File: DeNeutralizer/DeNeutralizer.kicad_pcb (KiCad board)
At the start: 2 copper layers, 27.9 x 72 mm, 21 parts, among them J1 Screw_Terminal_01x03, J2 Screw_Terminal_01x03, J3 Screw_Terminal_01x03, J4 Screw_Terminal_01x03, J5 Screw_Terminal_01x02, J6 Screw_Terminal_01x05, J7 Screw_Terminal_01x02, J8 Conn_01x02_Male, J9 Ripple-Cap, U1 PC817

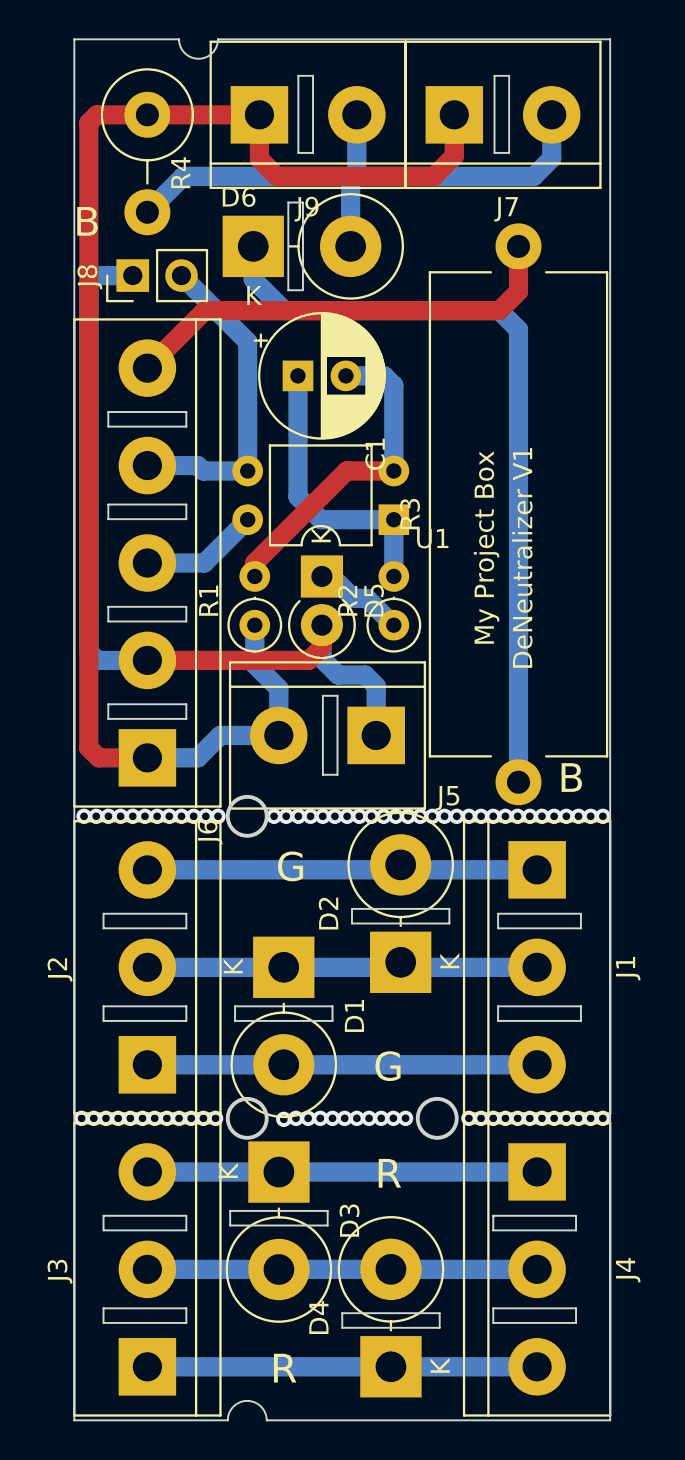
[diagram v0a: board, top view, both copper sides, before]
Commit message: Add Shelly 1 to the 3D model export
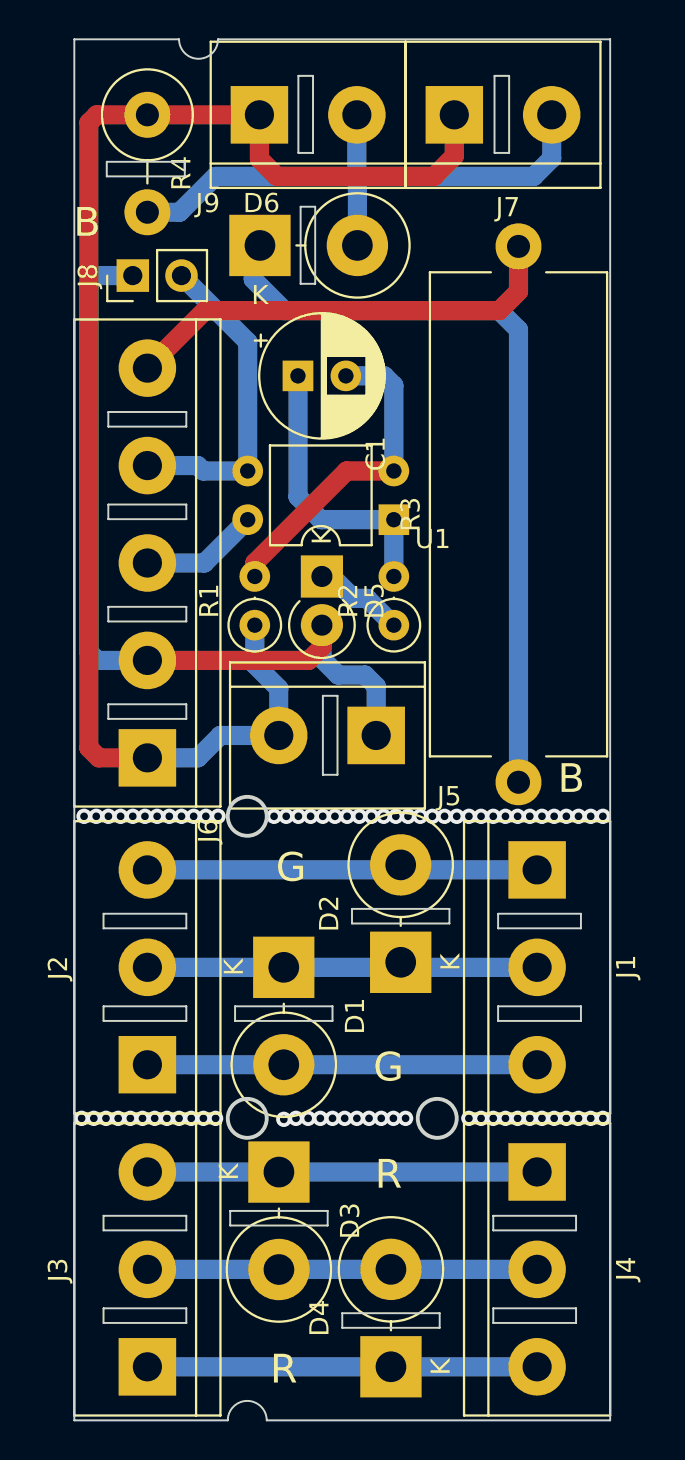
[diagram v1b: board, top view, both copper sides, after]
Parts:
- moved D6 0.35 mm to (126.5, 79.2)
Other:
- outline, holes or cut-outs redrawn
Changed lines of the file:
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@@
   (net 16 "Net-(J6-Pad4)")
   (footprint "Diode_THT:D_DO-201AD_P5.08mm_Vertical_KathodeUp" (layer "F.Cu")
-    (at 126.17 79.25)
+    (at 126.52 79.2)
     (descr "Diode, DO-201AD series, Axial, Vertical, pin pitch=5.08mm, , length*diameter=9.5*5.2mm^2, , http://www.diodes.com/_files/packages/DO-201AD.pdf")
     (tags "Diode DO-201AD series Axial Vertical pin pitch 5.08mm  length 9.5mm diameter 5.2mm")
@@
     (property "Sheetname" "")
     (attr through_hole)
-    (fp_text reference "D6" (at -0.762 -2.54) (layer "F.SilkS")
+    (fp_text reference "D6" (at 0.08 -2.2) (layer "F.SilkS")
       (effects (font (size 1 1) (thickness 0.15)))
     )
@@
       (effects (font (size 1 1) (thickness 0.15)))
     )
-    (fp_text user "${REFERENCE}" (at -0.762 -2.54) (layer "F.Fab")
+    (fp_text user "${REFERENCE}" (at 0.08 -2.2) (layer "F.Fab")
       (effects (font (size 1 1) (thickness 0.15)))
     )
@@
       (rotate (xyz 0 0 0))
     )
+    (model "C:/Users/POLYGONTeam/Desktop/Shelly_1_PM_Rund.stp"
+      (offset (xyz 10 25 15))
+      (scale (xyz 1 1 1))
+      (rotate (xyz 90 0 0))
+    )
   )
   (footprint "Diode_THT:D_DO-201AD_P5.08mm_Vertical_KathodeUp" (layer "F.Cu")
@@
     (property "Sheetname" "")
     (attr through_hole)
-    (fp_text reference "J9" (at 2.54 4.826) (layer "F.SilkS")
+    (fp_text reference "J9" (at -2.692 4.61) (layer "F.SilkS")
       (effects (font (size 1 1) (thickness 0.15)))
     )
@@
       (effects (font (size 1 1) (thickness 0.15)))
     )
-    (fp_text user "${REFERENCE}" (at 2.54 4.826) (layer "F.Fab")
+    (fp_text user "${REFERENCE}" (at -2.692 4.61) (layer "F.Fab")
       (effects (font (size 1 1) (thickness 0.15)))
     )
@@
   (gr_rect (start 138.684 134.62) (end 143.002 135.382) (layer "Edge.Cuts") (width 0.1) (fill none))
   (gr_rect (start 138.75 74.376) (end 139.512 70.358) (layer "Edge.Cuts") (width 0.1) (fill none))
+  (gr_rect (start 128.638 81.2) (end 129.4 77.182) (layer "Edge.Cuts") (width 0.1) (fill none))
   (gr_rect (start 118.364 134.62) (end 122.682 135.382) (layer "Edge.Cuts") (width 0.1) (fill none))
   (gr_line (start 124.841 140.462) (end 116.84 140.462) (layer "Edge.Cuts") (width 0.1))
@@
   (gr_circle (center 125.857 108.966) (end 126.873 108.966) (layer "Edge.Cuts") (width 0.2) (fill none))
   (gr_rect (start 130.81 134.874) (end 135.89 135.636) (layer "Edge.Cuts") (width 0.1) (fill none))
-  (gr_rect (start 128 81.536) (end 128.762 76.964) (layer "Edge.Cuts") (width 0.1) (fill none))
   (gr_rect (start 138.938 114.046) (end 143.256 114.808) (layer "Edge.Cuts") (width 0.1) (fill none))
   (gr_rect (start 118.364 114.046) (end 122.682 114.808) (layer "Edge.Cuts") (width 0.1) (fill none))
@@
   (gr_rect (start 125.222 118.872) (end 130.302 119.634) (layer "Edge.Cuts") (width 0.1) (fill none))
   (gr_rect (start 118.614 103.124) (end 122.682 103.886) (layer "Edge.Cuts") (width 0.1) (fill none))
+  (gr_rect (start 118.532 74.838) (end 122.6 75.6) (layer "Edge.Cuts") (width 0.1) (fill none))
   (gr_line (start 144.78 68.453) (end 124.333 68.453) (layer "Edge.Cuts") (width 0.1))
   (gr_rect (start 129.8 106.8) (end 130.562 102.682) (layer "Edge.Cuts") (width 0.1) (fill none))
@@
   (gr_rect (start 118.614 98.044) (end 122.682 98.806) (layer "Edge.Cuts") (width 0.1) (fill none))
   (gr_circle (center 135.763 124.714) (end 136.779 124.714) (layer "Edge.Cuts") (width 0.2) (fill none))
+  (gr_text "DeNeutralizer V1" (at 140.25 95.5 90) (layer "B.SilkS")
+    (effects (font (size 1 1) (thickness 0.25)) (justify mirror))
+  )
   (gr_text "N" (at 128.8 107.6) (layer "B.SilkS")
     (effects (font (size 1.5 1.5) (thickness 0.3)) (justify mirror))
@@
     (effects (font (size 1.5 1.5) (thickness 0.3)) (justify mirror))
   )
+  (gr_text "My Project Box" (at 138.25 95 90) (layer "B.SilkS")
+    (effects (font (size 1 1) (thickness 0.25)) (justify mirror))
+  )
   (gr_text "R" (at 127.762 137.795) (layer "F.SilkS")
     (effects (font (size 1.5 1.5) (thickness 0.3)))
   )
-  (gr_text "DeNeutralizer V1" (at 140.25 95.5 90) (layer "F.SilkS")
-    (effects (font (size 1 1) (thickness 0.25)))
-  )
   (gr_text "R" (at 133.223 127.635) (layer "F.SilkS")
     (effects (font (size 1.5 1.5) (thickness 0.3)))
@@
   (gr_text "B" (at 142.75 107) (layer "F.SilkS")
     (effects (font (size 1.5 1.5) (thickness 0.3)))
-  )
-  (gr_text "My Project Box" (at 138.25 95 90) (layer "F.SilkS")
-    (effects (font (size 1 1) (thickness 0.25)))
   )
   (gr_text "B" (at 117.5 78) (layer "F.SilkS")
@@
   (via (at 120.396 124.714) (size 0.8) (drill 0.4) (layers "F.Cu" "B.Cu") (free) (net 0))
   (via (at 131.572 124.714) (size 0.8) (drill 0.4) (layers "F.Cu" "B.Cu") (free) (net 0))
-  (via (at 117.348 108.966) (size 0.8) (drill 0.4) (layers "F.Cu" "B.Cu") (free) (net 0))
+  (via (at 117.348 108.966) (size 0.8) (drill 0.4) (layers "F.Cu" "B.Cu") (remove_unused_layers) (keep_end_layers) (free) (net 0))
   (via (at 121.158 108.966) (size 0.8) (drill 0.4) (layers "F.Cu" "B.Cu") (free) (net 0))
   (via (at 122.936 124.714) (size 0.8) (drill 0.4) (layers "F.Cu" "B.Cu") (free) (net 0))
@@
   (segment (start 139 82.6) (end 140 83.6) (width 1) (layer "B.Cu") (net 13))
   (segment (start 127.8 82.6) (end 139 82.6) (width 1) (layer "B.Cu") (net 13))
-  (segment (start 131.4 75.6) (end 122.52 75.6) (width 1) (layer "B.Cu") (net 14))
+  (segment (start 131.6 79.2) (end 131.6 75.8) (width 1) (layer "B.Cu") (net 14))
   (segment (start 140.8 75.6) (end 131.4 75.6) (width 1) (layer "B.Cu") (net 14))
   (segment (start 141.732 72.39) (end 141.732 74.668) (width 1) (layer "B.Cu") (net 14))
+  (segment (start 131.6 75.8) (end 131.4 75.6) (width 1) (layer "B.Cu") (net 14))
   (segment (start 141.732 74.668) (end 140.8 75.6) (width 1) (layer "B.Cu") (net 14))
-  (segment (start 131.25 75.75) (end 131.4 75.6) (width 1) (layer "B.Cu") (net 14))
-  (segment (start 122.52 75.6) (end 120.65 77.47) (width 1) (layer "B.Cu") (net 14))
+  (segment (start 124.2 75.6) (end 131.4 75.6) (width 1) (layer "B.Cu") (net 14))
   (segment (start 131.572 72.39) (end 131.572 75.428) (width 1) (layer "B.Cu") (net 14))
-  (segment (start 131.25 79.25) (end 131.25 75.75) (width 1) (layer "B.Cu") (net 14))
+  (segment (start 122.33 77.47) (end 124.2 75.6) (width 1) (layer "B.Cu") (net 14))
   (segment (start 131.572 75.428) (end 131.4 75.6) (width 1) (layer "B.Cu") (net 14))
+  (segment (start 120.65 77.47) (end 122.33 77.47) (width 1) (layer "B.Cu") (net 14))
   (segment (start 117.6 72.8) (end 118.01 72.39) (width 1) (layer "F.Cu") (net 15))
   (segment (start 126.492 72.39) (end 126.492 74.692) (width 1) (layer "F.Cu") (net 15))
